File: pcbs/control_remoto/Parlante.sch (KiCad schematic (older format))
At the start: 19 parts, among them J1 JACK_TRS_6PINS, U6 TL082, U7 LM386_mod

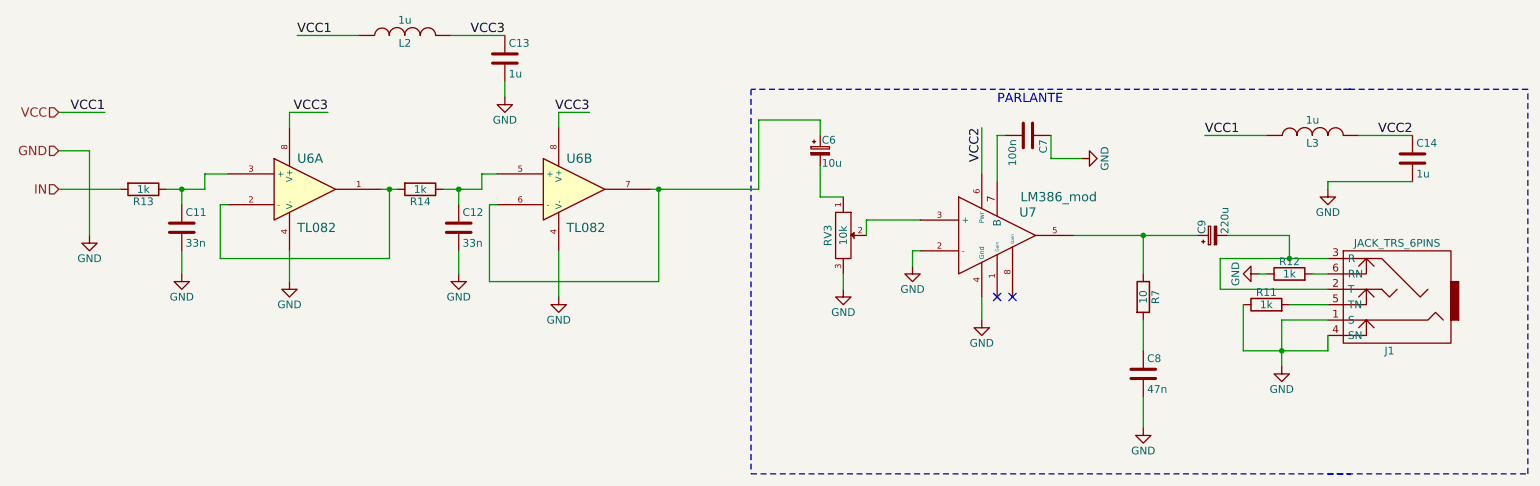
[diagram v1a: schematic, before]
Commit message: actualizo las 3 placas, revisar y mandar a fabricar
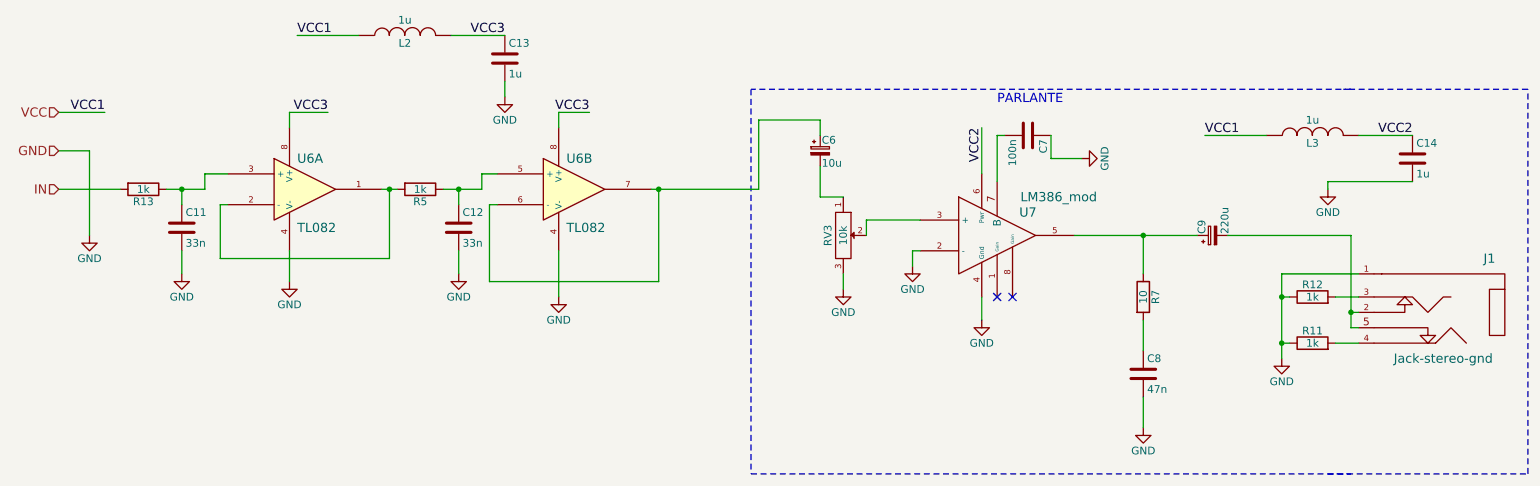
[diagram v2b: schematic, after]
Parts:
- removed J1: JACK_TRS_6PINS, Pin_Headers:Pin_Header_Angled_1x06, symbol JACK_TRS_6PINS
- added J1: Jack-stereo-gnd, Popurri_CDR:audio-jack-stereo, symbol Jack-stereo-gnd
- C11, C12: footprint Capacitors_ThroughHole:C_Disc_D3_P2.5 -> Capacitors_ThroughHole:C_Rect_L7_W2_P5
- C13, C14: footprint Capacitors_ThroughHole:C_Disc_D3_P2.5 -> Capacitors_ThroughHole:C_Rect_L18_W5_P15
- renumbered R14 to R5
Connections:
- net GND: now also J1.1
- net at C9.2: now also J1.2, J1.5
- net at R11.2: now also J1.4
- net at R12.2: now also J1.3
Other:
- moved on the sheet: R11, R12
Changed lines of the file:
@@
 LIBS:zigbit_dual
 LIBS:lm386_mod
+LIBS:audio-jack-stereo
 LIBS:controlremoto-cache
 EELAYER 25 0
@@
 	8000 3350 8000 3150
 Wire Wire Line
-	8550 2100 8950 2100
+	8550 2100 9350 2100
 $Comp
 L GND #PWR029
-U 1 1 55289C14
-P 8900 2950
-F 0 "#PWR029" H 8900 2700 50  0001 C CNN
-F 1 "GND" H 8900 2800 50  0000 C CNN
-F 2 "" H 8900 2950 60  0000 C CNN
-F 3 "" H 8900 2950 60  0000 C CNN
-	1    8900 2950
-	1    0    0    -1
-$EndComp
-$Comp
-L GND #PWR030
 U 1 1 55289CEE
 P 6050 2450
-F 0 "#PWR030" H 6050 2200 50  0001 C CNN
+F 0 "#PWR029" H 6050 2200 50  0001 C CNN
 F 1 "GND" H 6050 2300 50  0000 C CNN
 F 2 "" H 6050 2450 60  0000 C CNN
@@
 Wire Wire Line
 	5500 1350 5900 1350
-Wire Wire Line
-	8500 2250 9200 2250
-$Comp
-L JACK_TRS_6PINS J1
-U 1 1 552867E4
-P 9600 2450
-F 0 "J1" H 9600 2850 50  0000 C CNN
-F 1 "JACK_TRS_6PINS" H 9550 2150 50  0000 C CNN
-F 2 "Pin_Headers:Pin_Header_Angled_1x06" H 9700 2300 60  0001 C CNN
-F 3 "" H 9700 2300 60  0000 C CNN
-	1    9600 2450
-	-1   0    0    1
-$EndComp
-Wire Wire Line
-	8500 2450 9200 2450
 $Comp
 L R R11
 U 1 1 55286982
-P 8800 2550
-F 0 "R11" V 8880 2550 50  0000 C CNN
-F 1 "1k" V 8800 2550 50  0000 C CNN
-F 2 "Resistors_ThroughHole:Resistor_Horizontal_RM10mm" V 8730 2550 30  0001 C CNN
-F 3 "" H 8800 2550 30  0000 C CNN
-	1    8800 2550
+P 9100 2800
+F 0 "R11" V 9180 2800 50  0000 C CNN
+F 1 "1k" V 9100 2800 50  0000 C CNN
+F 2 "Resistors_ThroughHole:Resistor_Horizontal_RM10mm" V 9030 2800 30  0001 C CNN
+F 3 "" H 9100 2800 30  0000 C CNN
+	1    9100 2800
 	0    -1   -1   0
 $EndComp
 Wire Wire Line
-	9200 2850 9200 2750
-Wire Wire Line
-	9200 2550 8950 2550
-Wire Wire Line
-	8650 2550 8650 2850
-Wire Wire Line
-	8650 2850 9200 2850
-Wire Wire Line
-	9200 2650 8900 2650
-Wire Wire Line
-	8900 2650 8900 2950
-Connection ~ 8900 2850
-Wire Wire Line
-	8950 2100 8950 2250
-Connection ~ 8950 2250
+	9400 2800 9250 2800
 $Comp
 L R R12
 U 1 1 55286E6F
-P 8950 2350
-F 0 "R12" V 9030 2350 50  0000 C CNN
-F 1 "1k" V 8950 2350 50  0000 C CNN
-F 2 "Resistors_ThroughHole:Resistor_Horizontal_RM10mm" V 8880 2350 30  0001 C CNN
-F 3 "" H 8950 2350 30  0000 C CNN
-	1    8950 2350
+P 9100 2500
+F 0 "R12" V 9180 2500 50  0000 C CNN
+F 1 "1k" V 9100 2500 50  0000 C CNN
+F 2 "Resistors_ThroughHole:Resistor_Horizontal_RM10mm" V 9030 2500 30  0001 C CNN
+F 3 "" H 9100 2500 30  0000 C CNN
+	1    9100 2500
 	0    -1   -1   0
 $EndComp
 Wire Wire Line
-	9100 2350 9200 2350
-$Comp
-L GND #PWR031
+	9250 2500 9400 2500
+$Comp
+L GND #PWR030
 U 1 1 55287138
-P 8750 2350
-F 0 "#PWR031" H 8750 2100 50  0001 C CNN
-F 1 "GND" H 8750 2200 50  0000 C CNN
-F 2 "" H 8750 2350 60  0000 C CNN
-F 3 "" H 8750 2350 60  0000 C CNN
-	1    8750 2350
-	0    1    1    0
-$EndComp
-Wire Wire Line
-	8800 2350 8750 2350
-Wire Wire Line
-	8500 2250 8500 2450
+P 8900 2900
+F 0 "#PWR030" H 8900 2650 50  0001 C CNN
+F 1 "GND" H 8900 2750 50  0000 C CNN
+F 2 "" H 8900 2900 60  0000 C CNN
+F 3 "" H 8900 2900 60  0000 C CNN
+	1    8900 2900
+	1    0    0    -1
+$EndComp
 Wire Notes Line
 	9200 3650 10500 3650
@@
 F 0 "C14" H 9775 1700 50  0000 L CNN
 F 1 "1u" H 9775 1500 50  0000 L CNN
-F 2 "Capacitors_ThroughHole:C_Disc_D3_P2.5" H 9788 1450 30  0001 C CNN
+F 2 "Capacitors_ThroughHole:C_Rect_L18_W5_P15" H 9788 1450 30  0001 C CNN
 F 3 "" H 9750 1600 60  0000 C CNN
 	1    9750 1600
@@
 VCC2
 $Comp
-L GND #PWR032
+L GND #PWR031
 U 1 1 552879C2
 P 9200 1800
-F 0 "#PWR032" H 9200 1550 50  0001 C CNN
+F 0 "#PWR031" H 9200 1550 50  0001 C CNN
 F 1 "GND" H 9200 1650 50  0000 C CNN
 F 2 "" H 9200 1800 60  0000 C CNN
@@
 	1150 1550 1150 2100
 $Comp
-L GND #PWR033
+L GND #PWR032
 U 1 1 552885DB
 P 1150 2100
-F 0 "#PWR033" H 1150 1850 50  0001 C CNN
+F 0 "#PWR032" H 1150 1850 50  0001 C CNN
 F 1 "GND" H 1150 1950 50  0000 C CNN
 F 2 "" H 1150 2100 60  0000 C CNN
@@
 F 0 "C13" H 3875 1050 50  0000 L CNN
 F 1 "1u" H 3875 850 50  0000 L CNN
-F 2 "Capacitors_ThroughHole:C_Disc_D3_P2.5" H 3888 800 30  0001 C CNN
+F 2 "Capacitors_ThroughHole:C_Rect_L18_W5_P15" H 3888 800 30  0001 C CNN
 F 3 "" H 3850 950 60  0000 C CNN
 	1    3850 950
@@
 VCC3
 $Comp
-L GND #PWR034
+L GND #PWR033
 U 1 1 552E0502
 P 3850 1200
-F 0 "#PWR034" H 3850 950 50  0001 C CNN
+F 0 "#PWR033" H 3850 950 50  0001 C CNN
 F 1 "GND" H 3850 1050 50  0000 C CNN
 F 2 "" H 3850 1200 60  0000 C CNN
@@
 VCC3
 $Comp
-L GND #PWR035
+L GND #PWR034
 U 1 1 552E0670
 P 2450 2400
-F 0 "#PWR035" H 2450 2150 50  0001 C CNN
+F 0 "#PWR034" H 2450 2150 50  0001 C CNN
 F 1 "GND" H 2450 2250 50  0000 C CNN
 F 2 "" H 2450 2400 60  0000 C CNN
@@
 F 0 "C11" H 1775 2150 50  0000 L CNN
 F 1 "33n" H 1775 1950 50  0000 L CNN
-F 2 "Capacitors_ThroughHole:C_Disc_D3_P2.5" H 1788 1900 30  0001 C CNN
+F 2 "Capacitors_ThroughHole:C_Rect_L7_W2_P5" H 1788 1900 30  0001 C CNN
 F 3 "" H 1750 2050 60  0000 C CNN
 	1    1750 2050
@@
 	1750 2200 1750 2350
 $Comp
-L GND #PWR036
+L GND #PWR035
 U 1 1 552E0A9C
 P 1750 2350
-F 0 "#PWR036" H 1750 2100 50  0001 C CNN
+F 0 "#PWR035" H 1750 2100 50  0001 C CNN
 F 1 "GND" H 1750 2200 50  0000 C CNN
 F 2 "" H 1750 2350 60  0000 C CNN
@@
 	4850 2400 4850 1800
 $Comp
-L R R14
+L R R5
 U 1 1 552E0E36
 P 3300 1800
-F 0 "R14" V 3380 1800 50  0000 C CNN
+F 0 "R5" V 3380 1800 50  0000 C CNN
 F 1 "1k" V 3300 1800 50  0000 C CNN
 F 2 "Resistors_ThroughHole:Resistor_Horizontal_RM10mm" V 3230 1800 30  0001 C CNN
@@
 F 0 "C12" H 3575 2150 50  0000 L CNN
 F 1 "33n" H 3575 1950 50  0000 L CNN
-F 2 "Capacitors_ThroughHole:C_Disc_D3_P2.5" H 3588 1900 30  0001 C CNN
+F 2 "Capacitors_ThroughHole:C_Rect_L7_W2_P5" H 3588 1900 30  0001 C CNN
 F 3 "" H 3550 2050 60  0000 C CNN
 	1    3550 2050
@@
 	3550 2200 3550 2350
 $Comp
-L GND #PWR037
+L GND #PWR036
 U 1 1 552E0E46
 P 3550 2350
-F 0 "#PWR037" H 3550 2100 50  0001 C CNN
+F 0 "#PWR036" H 3550 2100 50  0001 C CNN
 F 1 "GND" H 3550 2200 50  0000 C CNN
 F 2 "" H 3550 2350 60  0000 C CNN
@@
 	4200 2200 4200 2500
 $Comp
-L GND #PWR038
+L GND #PWR037
 U 1 1 552E12B9
 P 4200 2500
-F 0 "#PWR038" H 4200 2250 50  0001 C CNN
+F 0 "#PWR037" H 4200 2250 50  0001 C CNN
 F 1 "GND" H 4200 2350 50  0000 C CNN
 F 2 "" H 4200 2500 60  0000 C CNN
@@
 	0    -1   -1   0
 $EndComp
+$Comp
+L Jack-stereo-gnd J1
+U 1 1 5535BCC6
+P 9850 2600
+F 0 "J1" H 10250 2950 60  0000 C CNN
+F 1 "Jack-stereo-gnd" H 9950 2300 60  0000 C CNN
+F 2 "Popurri_CDR:audio-jack-stereo" H 9850 2250 60  0001 C CNN
+F 3 "" H 9850 2250 60  0000 C CNN
+	1    9850 2600
+	1    0    0    -1
+$EndComp
+Wire Wire Line
+	8900 2350 8900 2900
+Wire Wire Line
+	8900 2350 9400 2350
+Connection ~ 8900 2500
+Wire Wire Line
+	9350 2100 9350 2700
+Wire Wire Line
+	9350 2700 9400 2700
+Wire Wire Line
+	9400 2600 9350 2600
+Connection ~ 9350 2600
+Wire Wire Line
+	8900 2800 8950 2800
+Connection ~ 8900 2800
+Wire Wire Line
+	8950 2500 8900 2500
 $EndSCHEMATC
